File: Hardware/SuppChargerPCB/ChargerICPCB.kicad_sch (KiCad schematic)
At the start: 44 parts, among them J1 SLIMSTACK, J2 SLIMSTACK, Q1 NMOS, Q2 PMOS, U1 LTC4011CFE

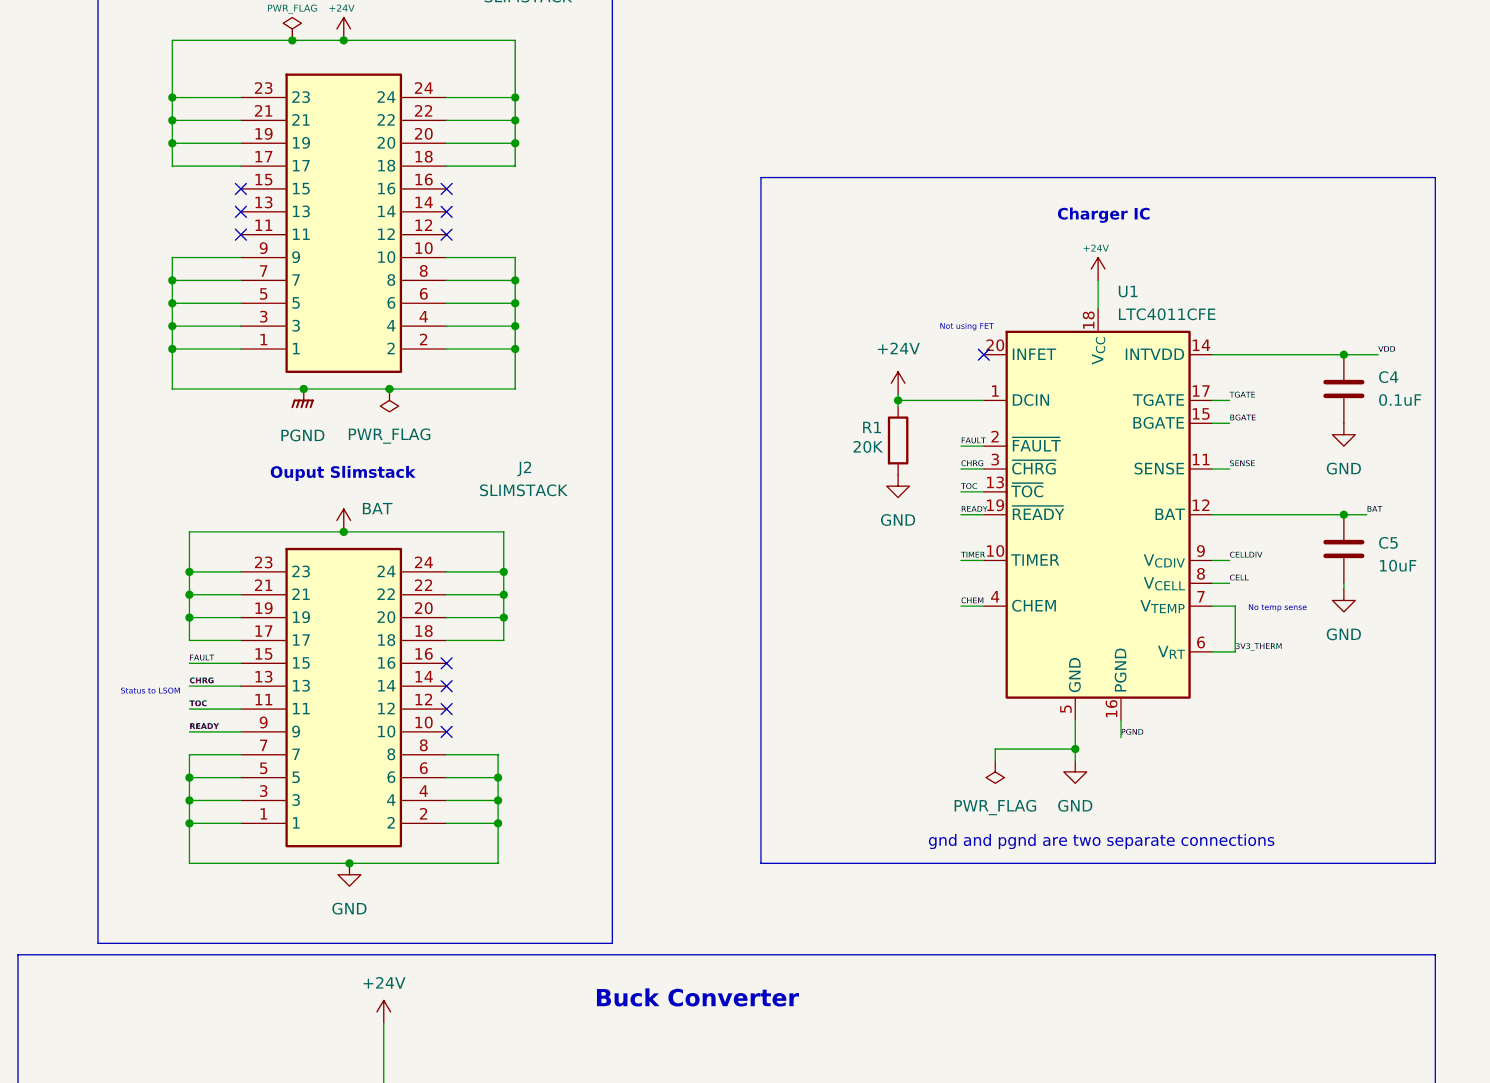
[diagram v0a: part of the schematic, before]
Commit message: fixed pinout
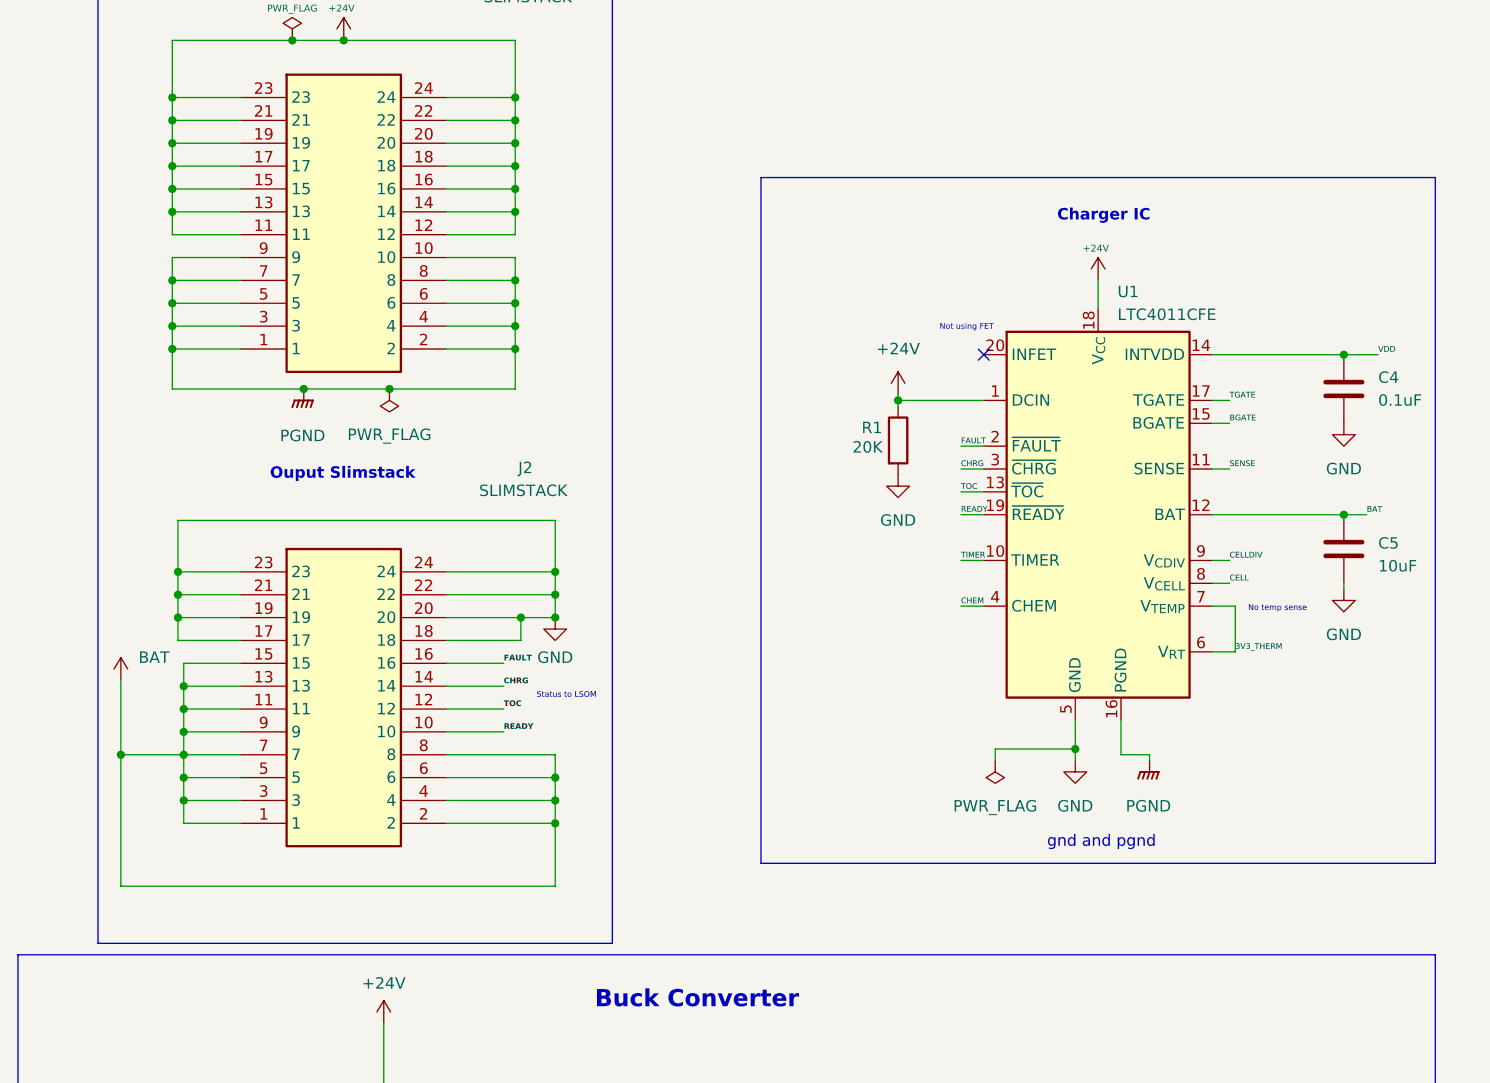
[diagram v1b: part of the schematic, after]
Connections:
- net +24V: now also J1.11, J1.12, J1.13, J1.14, J1.15, J1.16
- net BAT: now also J2.1, J2.11, J2.13, J2.15, J2.2, J2.3, J2.4, J2.5, J2.6, J2.7, J2.8, J2.9; no longer J2.17, J2.18, J2.19, J2.20, J2.21, J2.22, J2.23, J2.24
- net CHRG: now also J2.14; no longer J2.13
- net FAULT: now also J2.16; no longer J2.15
- net GND: now also J2.17, J2.18, J2.19, J2.20, J2.21, J2.22, J2.23, J2.24; no longer J2.1, J2.2, J2.3, J2.4, J2.5, J2.6, J2.7, J2.8
- net READY: now also J2.10; no longer J2.9
- net TOC: now also J2.12; no longer J2.11
- no-connect marks 11 -> 1
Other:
- note added: "gnd and pgnd"
- note removed: "gnd and pgnd are two separate connections"
